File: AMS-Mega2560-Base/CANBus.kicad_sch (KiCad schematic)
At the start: 4 parts, among them IC2 MCP2542FD-H_SN, IC3 MCP2518FDT-E_SL

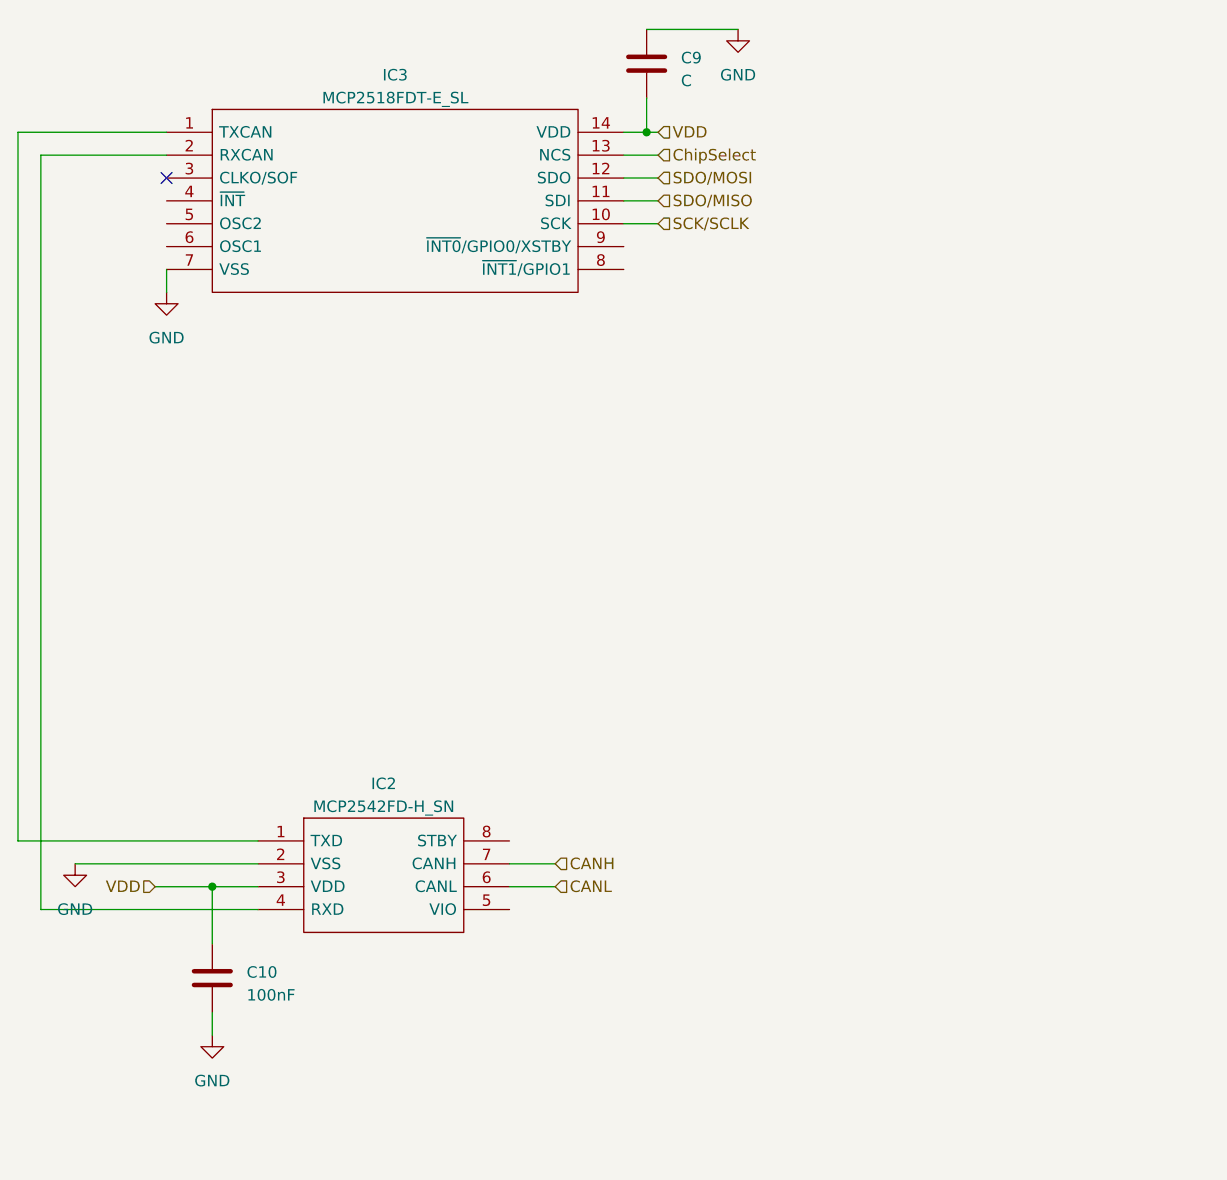
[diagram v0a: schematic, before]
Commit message: finished CAN section. inputs need to be fixed.
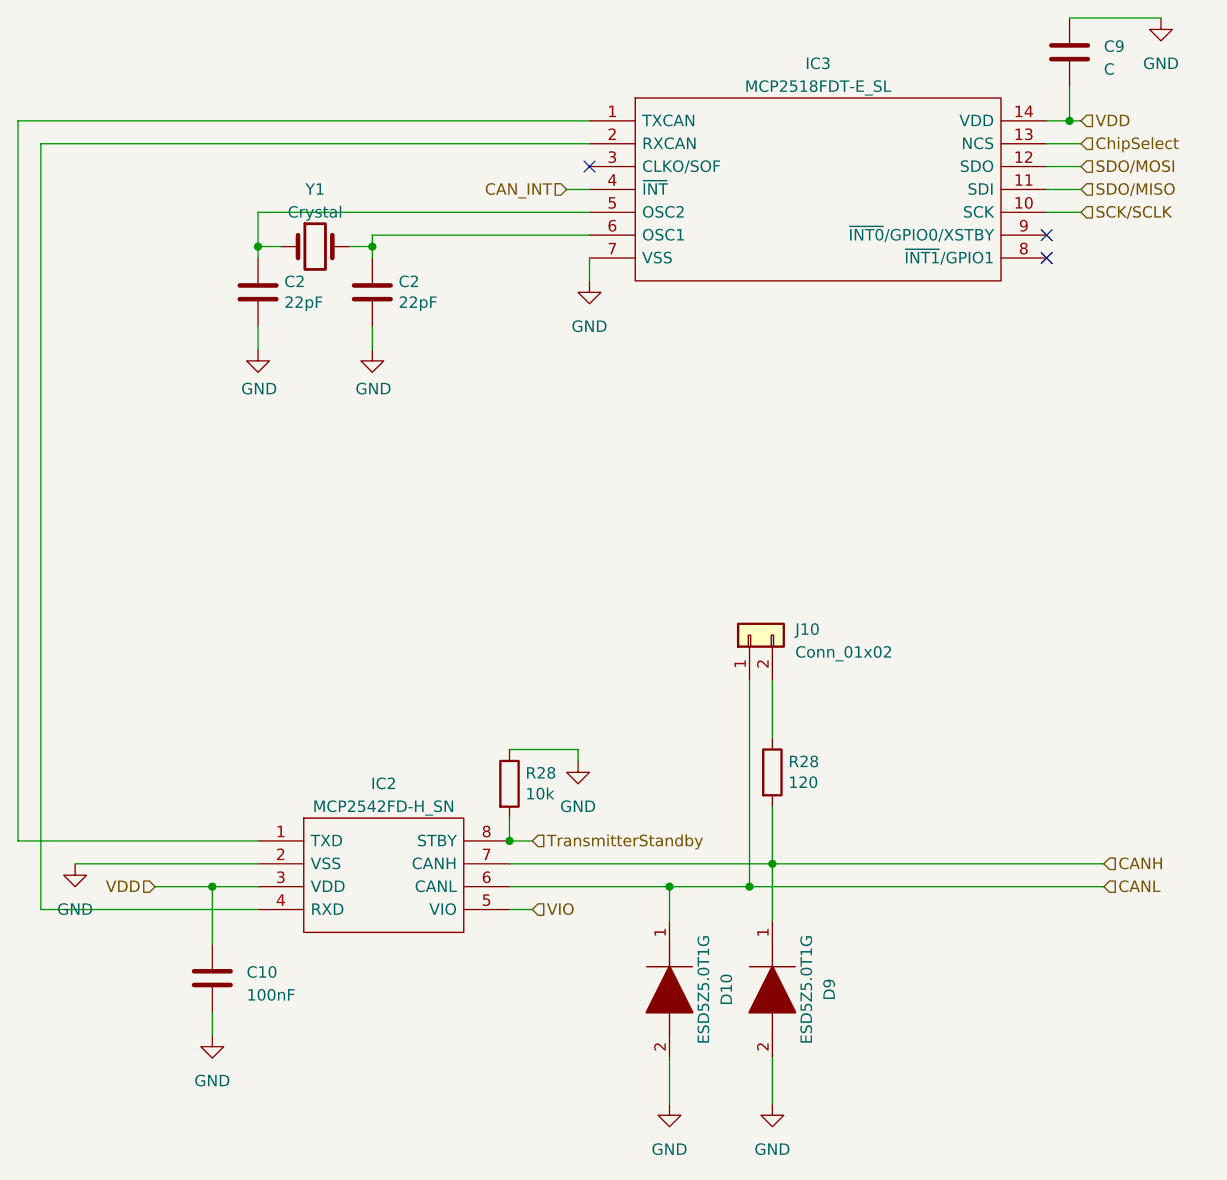
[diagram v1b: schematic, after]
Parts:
- added C2 (x2): 22pF, Capacitor_THT:C_Disc_D5.1mm_W3.2mm_P5.00mm, symbol Device:C
- added D10, D9: ESD5Z5.0T1G, SODFL1608X70N, symbol SamacSys_Parts:ESD5Z5.0T1G
- added J10: Conn_01x02, symbol Connector_Generic:Conn_01x02
- added R28: 10k, Resistor_THT:R_Axial_DIN0207_L6.3mm_D2.5mm_P2.54mm_Vertical, symbol Device:R
- added R28: 120, Resistor_THT:R_Axial_DIN0207_L6.3mm_D2.5mm_P2.54mm_Vertical, symbol Device:R
- added Y1: Crystal, Crystal:Crystal_HC49-U_Vertical, symbol Device:Crystal
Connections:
- net CANH: now also D9.1, R28.2
- net CANL: now also D10.1, J10.1 (Pin_1)
- net GND: now also C2.2, C2.2, D10.2, D9.2, R28.1
- net VIO: now reaches IC2.5 (VIO)
- net TransmitterStandby: now reaches IC2.8 (STBY)
- net TransmitterStandby: now also R28.2
- net CAN_INT: now reaches IC3.4 (~{INT})
- net at IC3.5 (OSC2): now also C2.1, Y1.1
- net at IC3.6 (OSC1): now also C2.1, Y1.2
- new net: J10.2 (Pin_2), R28.1
- no-connect marks 1 -> 3
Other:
- moved on the sheet: C9, IC3

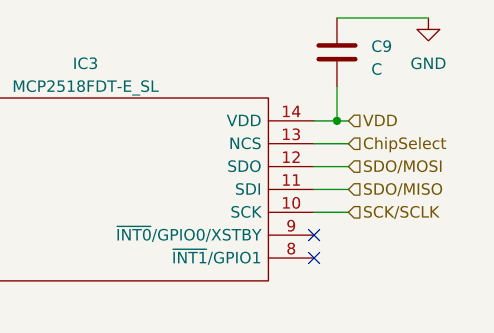
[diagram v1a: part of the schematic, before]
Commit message: * Schematic ** finished CAN bus Design work ** updated the input circuits to my standard design and removed the old one that was funky
* PCB
** updated footprints
** removed the old parts/designed
** starting prep for placing parts
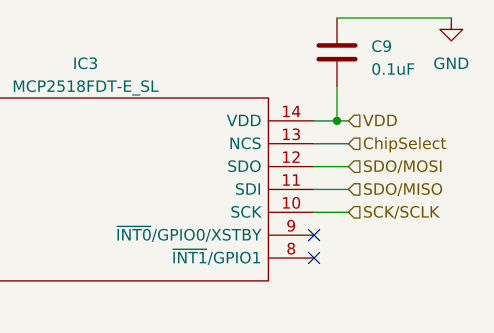
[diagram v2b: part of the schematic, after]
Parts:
- C10: footprint (none) -> Capacitor_THT:C_Disc_D5.1mm_W3.2mm_P5.00mm
- C9: value C -> 0.1uF; footprint (none) -> Capacitor_THT:C_Disc_D5.1mm_W3.2mm_P5.00mm
- D10, D9: footprint SODFL1608X70N -> SamacSys_Parts:SODFL1608X70N
- IC2: footprint SOIC127P600X175-8N -> SamacSys_Parts:SOIC127P600X175-8N
- IC3: footprint SOIC127P600X175-14N -> SamacSys_Parts:SOIC127P600X175-14N
- J10: footprint (none) -> Connector_PinHeader_2.54mm:PinHeader_1x02_P2.54mm_Vertical
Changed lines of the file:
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@@
     (stroke (width 0) (type default))
   )
-  (wire (pts (xy 196.85 48.26) (xy 207.01 48.26))
+  (wire (pts (xy 196.85 48.26) (xy 209.55 48.26))
     (stroke (width 0) (type default))
   )
@@
       (effects (font (size 1.27 1.27)))
     )
-    (property "Footprint" "SODFL1608X70N" (at 163.83 160.02 0)
+    (property "Footprint" "SamacSys_Parts:SODFL1608X70N" (at 163.83 160.02 0)
       (effects (font (size 1.27 1.27)) (justify left) hide)
     )
@@
       (effects (font (size 1.27 1.27)))
     )
-    (property "Footprint" "SOIC127P600X175-8N" (at 130.81 137.16 0)
+    (property "Footprint" "SamacSys_Parts:SOIC127P600X175-8N" (at 130.81 137.16 0)
       (effects (font (size 1.27 1.27)) (justify left) hide)
     )
@@
       (effects (font (size 1.27 1.27)) (justify right))
     )
-    (property "Footprint" "" (at 161.29 116.84 0)
+    (property "Footprint" "Connector_PinHeader_2.54mm:PinHeader_1x02_P2.54mm_Vertical" (at 161.29 116.84 0)
       (effects (font (size 1.27 1.27)) hide)
     )
@@
       (effects (font (size 1.27 1.27)) (justify left))
     )
-    (property "Footprint" "" (at 102.5652 158.75 0)
+    (property "Footprint" "Capacitor_THT:C_Disc_D5.1mm_W3.2mm_P5.00mm" (at 102.5652 158.75 0)
       (effects (font (size 1.27 1.27)) hide)
     )
@@
       (effects (font (size 1.27 1.27)))
     )
-    (property "Footprint" "SOIC127P600X175-14N" (at 190.5 57.15 0)
+    (property "Footprint" "SamacSys_Parts:SOIC127P600X175-14N" (at 190.5 57.15 0)
       (effects (font (size 1.27 1.27)) (justify left) hide)
     )
@@
     )
   )
-  (symbol (lib_id "power:GND") (at 207.01 48.26 0) (unit 1)
-    (in_bom yes) (on_board yes) (dnp no) (fields_autoplaced)
-    (property "Reference" "#PWR062" (at 207.01 54.61 0)
-      (effects (font (size 1.27 1.27)) hide)
-    )
-    (property "Value" "GND" (at 207.01 53.34 0)
-      (effects (font (size 1.27 1.27)))
-    )
-    (property "Footprint" "" (at 207.01 48.26 0)
-      (effects (font (size 1.27 1.27)) hide)
-    )
-    (property "Datasheet" "" (at 207.01 48.26 0)
+  (symbol (lib_id "power:GND") (at 209.55 48.26 0) (unit 1)
+    (in_bom yes) (on_board yes) (dnp no) (fields_autoplaced)
+    (property "Reference" "#PWR062" (at 209.55 54.61 0)
+      (effects (font (size 1.27 1.27)) hide)
+    )
+    (property "Value" "GND" (at 209.55 53.34 0)
+      (effects (font (size 1.27 1.27)))
+    )
+    (property "Footprint" "" (at 209.55 48.26 0)
+      (effects (font (size 1.27 1.27)) hide)
+    )
+    (property "Datasheet" "" (at 209.55 48.26 0)
       (effects (font (size 1.27 1.27)) hide)
     )
@@
       (effects (font (size 1.27 1.27)))
     )
-    (property "Footprint" "SODFL1608X70N" (at 152.4 160.02 0)
+    (property "Footprint" "SamacSys_Parts:SODFL1608X70N" (at 152.4 160.02 0)
       (effects (font (size 1.27 1.27)) (justify left) hide)
     )
@@
       (effects (font (size 1.27 1.27)) (justify left))
     )
-    (property "Value" "C" (at 200.66 53.975 0)
-      (effects (font (size 1.27 1.27)) (justify left))
-    )
-    (property "Footprint" "" (at 197.8152 55.88 0)
-      (effects (font (size 1.27 1.27)) hide)
-    )
+    (property "Value" "0.1uF" (at 200.66 53.975 0)
+      (effects (font (size 1.27 1.27)) (justify left))
+    )
+    (property "Footprint" "Capacitor_THT:C_Disc_D5.1mm_W3.2mm_P5.00mm" (at 197.8152 55.88 0)
+      (effects (font (size 1.27 1.27)) hide)
+    )
